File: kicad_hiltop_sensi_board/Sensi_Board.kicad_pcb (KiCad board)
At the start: 4 copper layers, 159.6 x 100 mm, 459 parts, among them J1 Conn_02x06_Top_Bottom, J10 Conn_01x04, J11 Conn_02x10_Counter_Clockwise, J2 Conn_02x06_Top_Bottom, J3 Conn_03x32_DIN41612, J4 Conn_02x06_Top_Bottom, J5 Conn_02x06_Top_Bottom, J6 Conn_02x06_Top_Bottom, J7 Conn_02x07_Top_Bottom, J8 Conn_02x07_Top_Bottom, J9 Conn_02x05_Odd_Even, K1 HRS1KH-S, Q10 ZXMN6A07F, Q11 ZXMN6A07F, Q2 ZXMN6A07F, Q7 ZXMN6A07F, Q8 ZXMN6A07F, SW1 SW_Push, SW2 SW_DIP_x04, SW3 SW_DIP_x04, SW4 SW_DIP_x04, SW5 SW_DIP_x04, U1 INA250A4, U10 MAX31865, U11 MAX31865, U12 MAX4194, U13 CP2102N-A01-GQFN24, U14 BTS4140N, U15 BTS4140N, U16 MAX4194, U17 BTS4140N, U18 BTS4140N, U19 MAX4194, U2 LD1117S33TR_SOT223, U20 MAX4194, U21 MAX4194, U22 STM32F072RBTx, U23 MAX4194, U24 MAX4194, U25 MAX4194, U26 M74VHC1GT14DFT2G, U27 USB2502, U3 AT25DN512CSSHF-B, U4 AD8646, U5 AD8646, U6 LM75B, U7 DNF, U8 MAX31865, U9 MAX31865, Y1 50ppm 24.000MHZ, Y2 8MHZ, Y3 ABS25-32.768KHZ-6-T

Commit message: Sensi Board RevB
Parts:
- added R172: DNF, Resistor_SMD:R_0603_1608Metric, F.Cu at (118.5, 62.0)
- turned D2 to 180 degrees
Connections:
- D2 pad 1: +5V -> Net-(D2-Pad1)
- D2 pad 2: Net-(D2-Pad2) -> +5V
- R48 pad 2: Net-(D2-Pad2) -> Net-(D2-Pad1)
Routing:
- net +3V3: track 253.7 -> 256.3 mm, vias 73 -> 74
- net /STM_BOOT0_OUT: track 50.3 -> 52.5 mm
- net Net-(D2-Pad2): track 1.83 -> 0.00 mm
- net Net-(D2-Pad1): track 0.00 -> 1.83 mm

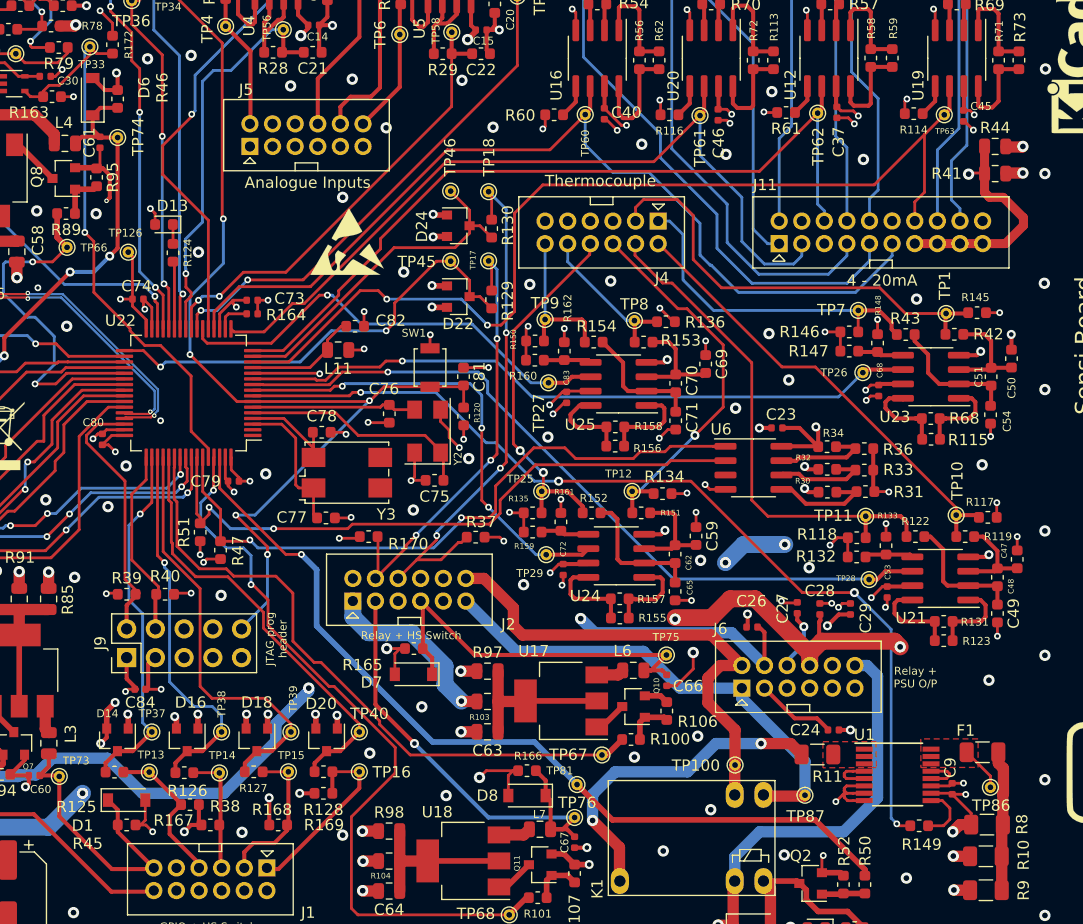
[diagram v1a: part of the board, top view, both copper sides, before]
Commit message: updated footprints to simplify bom
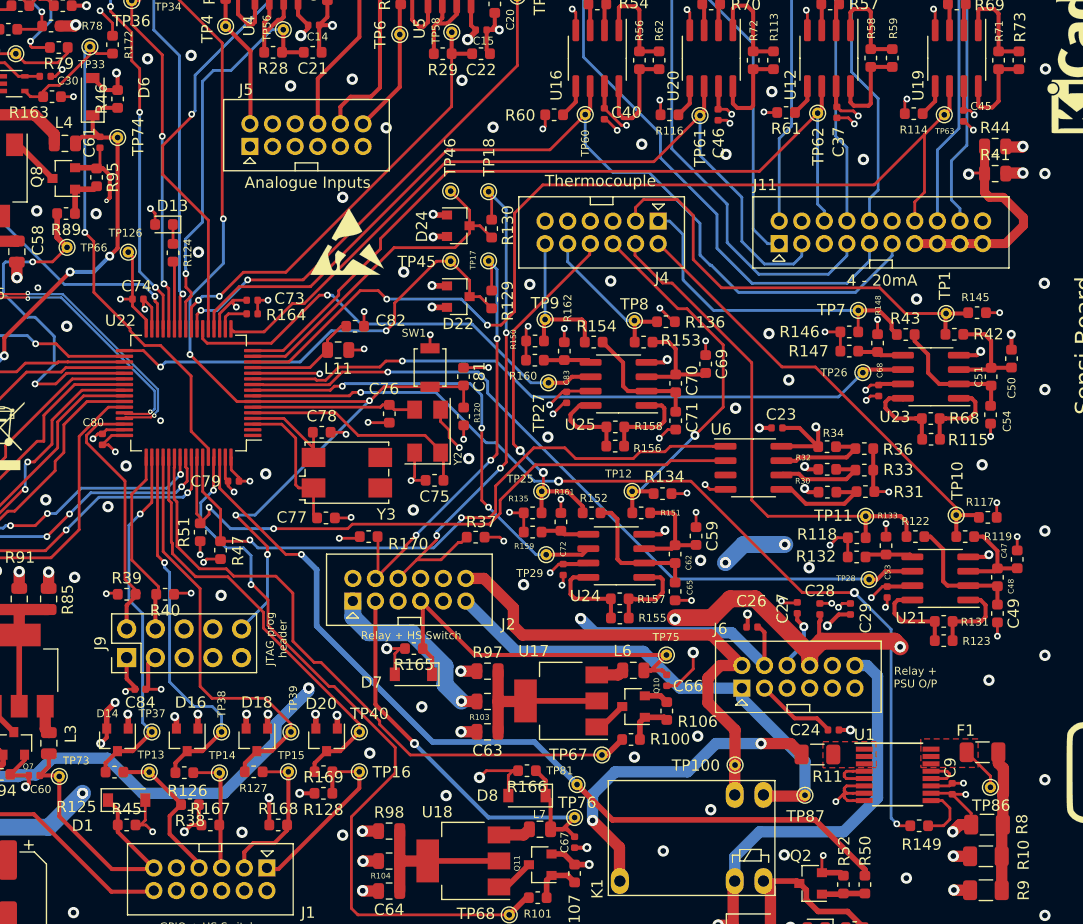
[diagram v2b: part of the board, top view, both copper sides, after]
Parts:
- C100, C103, C105: value 4.7uF -> 4.7uF
- C101, C37, C40, C45, C46, C53, C68, C72, C83, C90, C92, C94, C95, C96, C97, C98, C99: value 0.1uF -> 100nF
- R165, R166, R39, R40, R45, R46: value 100k -> 100K; footprint Capacitor_SMD:C_0603_1608Metric -> Resistor_SMD:R_0603_1608Metric
- R167, R168, R169, R38: footprint Capacitor_SMD:C_0603_1608Metric -> Resistor_SMD:R_0603_1608Metric
- R41, R44: footprint Capacitor_SMD:C_0805_2012Metric -> Resistor_SMD:R_0805_2012Metric
- R47, R51: value 4.7K -> 4K7
- R75: value 10K -> 10K
- R77: value 10k -> 10K

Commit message: fiducials added to pcb
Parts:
- added REF**: Fiducial_1mm_Mask2mm, Fiducial:Fiducial_1mm_Mask2mm, F.Cu at (204.1, 50.5)
- added REF**: Fiducial_1mm_Mask2mm, Fiducial:Fiducial_1mm_Mask2mm, F.Cu at (204.1, 140.7)
- added REF**: Fiducial_1mm_Mask2mm, Fiducial:Fiducial_1mm_Mask2mm, F.Cu at (64.2, 50.5)
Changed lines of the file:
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@@
     (tracks 3795)
     (zones 0)
-    (modules 460)
+    (modules 463)
     (nets 241)
   )
@@
     (uvia_drill 0.1)
   )
+  (module Fiducial:Fiducial_1mm_Mask2mm locked (layer F.Cu)
+    (at 204.1 50.45)
+    (descr "Circular Fiducial, 1mm bare copper, 2mm soldermask opening (Level A)")
+    (tags fiducial)
+    (attr smd)
+    (fp_text reference REF** (at 0 -2) (layer F.SilkS) hide
+      (effects (font (size 1 1) (thickness 0.15)))
+    )
+    (fp_text value Fiducial_1mm_Mask2mm (at 0 2) (layer F.Fab)
+      (effects (font (size 1 1) (thickness 0.15)))
+    )
+    (fp_circle (center 0 0) (end 1.25 0) (layer F.CrtYd) (width 0.05))
+    (fp_text user %R (at 0 0) (layer F.Fab)
+      (effects (font (size 0.4 0.4) (thickness 0.06)))
+    )
+    (fp_circle (center 0 0) (end 1 0) (layer F.Fab) (width 0.1))
+    (pad "" smd circle (at 0 0) (size 1 1) (layers F.Cu F.Mask)
+      (solder_mask_margin 0.5) (clearance 0.5))
+  )
+  (module Fiducial:Fiducial_1mm_Mask2mm locked (layer F.Cu)
+    (at 204.1 140.7)
+    (descr "Circular Fiducial, 1mm bare copper, 2mm soldermask opening (Level A)")
+    (tags fiducial)
+    (attr smd)
+    (fp_text reference REF** (at 0 -2) (layer F.SilkS) hide
+      (effects (font (size 1 1) (thickness 0.15)))
+    )
+    (fp_text value Fiducial_1mm_Mask2mm (at 0 2) (layer F.Fab)
+      (effects (font (size 1 1) (thickness 0.15)))
+    )
+    (fp_circle (center 0 0) (end 1 0) (layer F.Fab) (width 0.1))
+    (fp_text user %R (at 0 0) (layer F.Fab)
+      (effects (font (size 0.4 0.4) (thickness 0.06)))
+    )
+    (fp_circle (center 0 0) (end 1.25 0) (layer F.CrtYd) (width 0.05))
+    (pad "" smd circle (at 0 0) (size 1 1) (layers F.Cu F.Mask)
+      (solder_mask_margin 0.5) (clearance 0.5))
+  )
+  (module Fiducial:Fiducial_1mm_Mask2mm locked (layer F.Cu)
+    (at 64.15 50.45)
+    (descr "Circular Fiducial, 1mm bare copper, 2mm soldermask opening (Level A)")
+    (tags fiducial)
+    (attr smd)
+    (fp_text reference REF** (at 0 -2) (layer F.SilkS) hide
+      (effects (font (size 1 1) (thickness 0.15)))
+    )
+    (fp_text value Fiducial_1mm_Mask2mm (at 0 2) (layer F.Fab)
+      (effects (font (size 1 1) (thickness 0.15)))
+    )
+    (fp_circle (center 0 0) (end 1.25 0) (layer F.CrtYd) (width 0.05))
+    (fp_text user %R (at 0 0) (layer F.Fab)
+      (effects (font (size 0.4 0.4) (thickness 0.06)))
+    )
+    (fp_circle (center 0 0) (end 1 0) (layer F.Fab) (width 0.1))
+    (pad "" smd circle (at 0 0) (size 1 1) (layers F.Cu F.Mask)
+      (solder_mask_margin 0.5) (clearance 0.5))
+  )
   (module Connector_PinHeader_1.27mm:PinHeader_1x02_P1.27mm_Vertical (layer F.Cu)
